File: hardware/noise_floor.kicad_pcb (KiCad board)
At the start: 2 copper layers, 51.5 x 62.1 mm, 14 parts, among them J1 Input, J2 Output, J3 DC Power, J4 IO/Effect Connector 1 (IO Sid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, J5 IO/Effect Connector 2 (IO Sid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, J6 IO/Switch Connector 1 (IO Sid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, J7 IO/Switch Connector 2 (IO Sid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, J8 IO/Switch Connector 1 (Switch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, J9 IO/Switch Connector 2 (Switch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, SW1 Footswitch

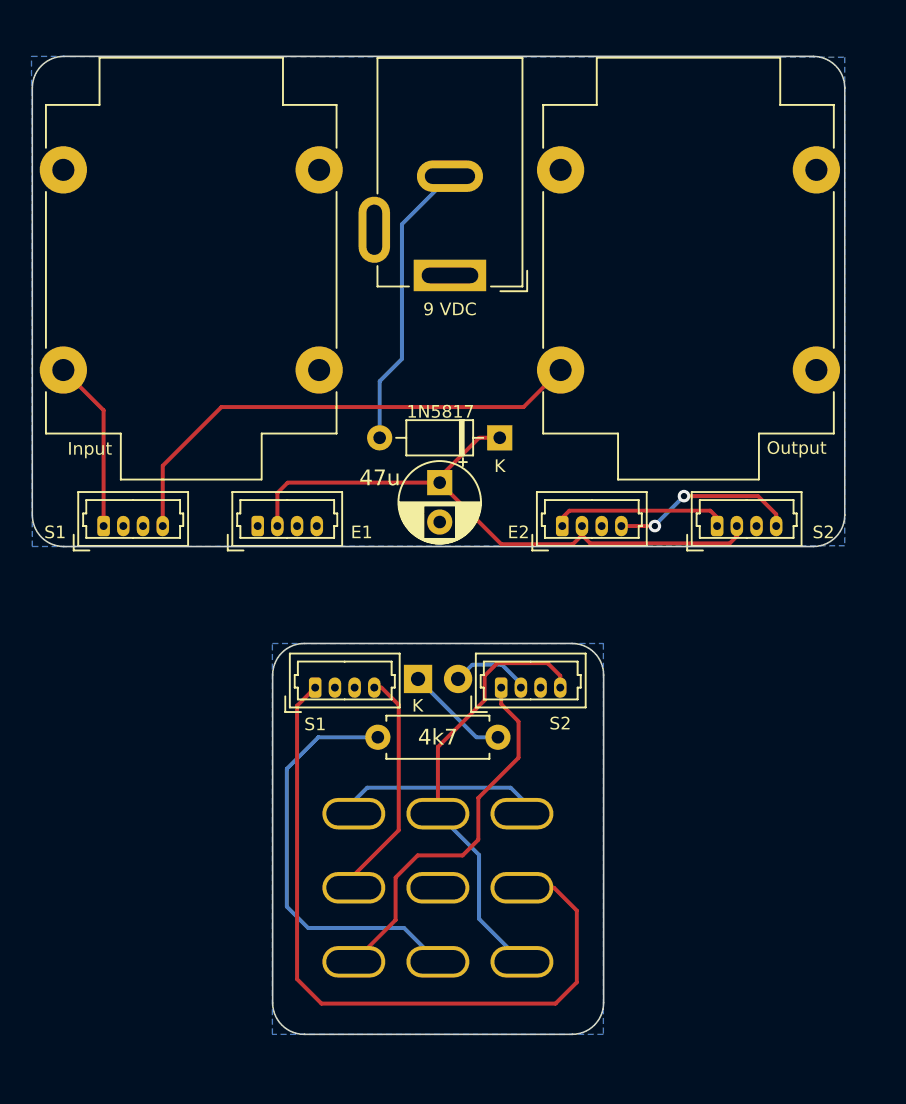
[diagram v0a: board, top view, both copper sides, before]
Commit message: v0.03 updates:
 - switch to SMD resistor and diode to save space (particularly on footswitch board)
 - move IO and DC jacks to bottom of board and ensure they're on the correct side
 - consolidate to a single effect board connector.
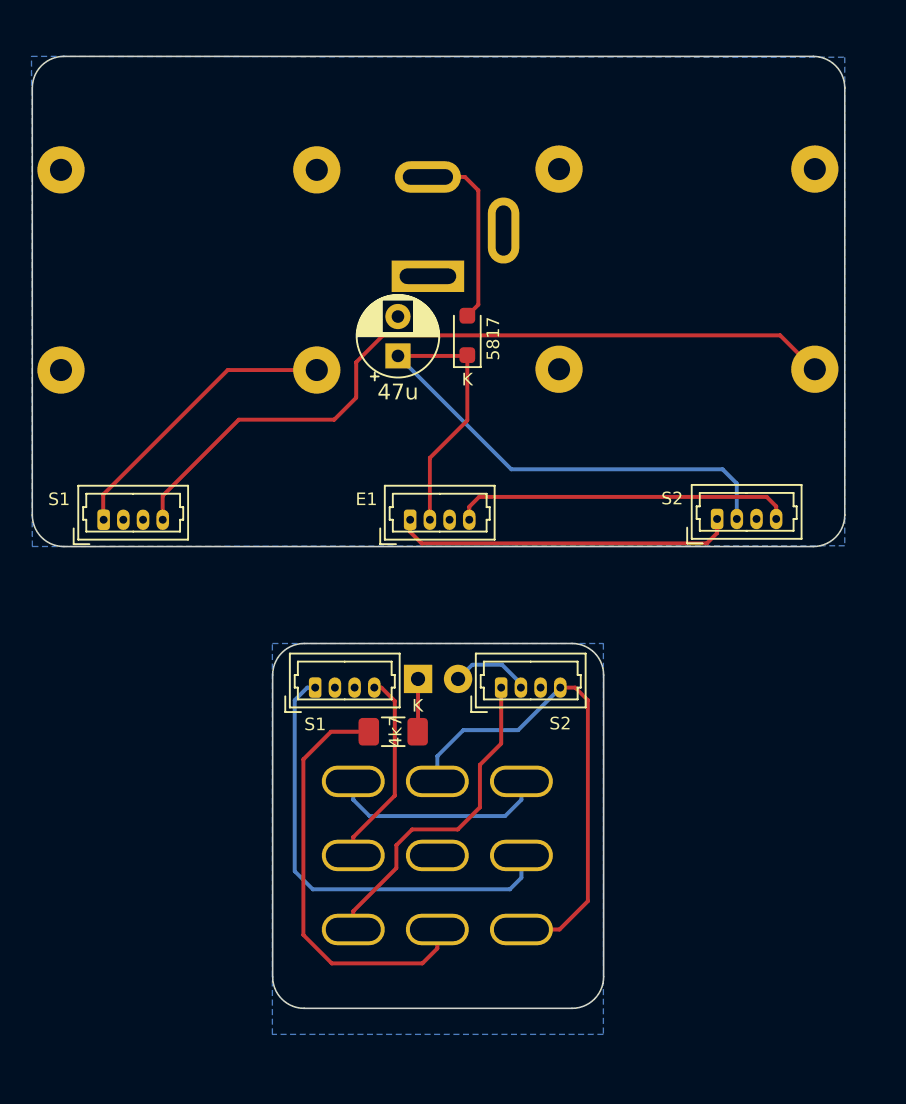
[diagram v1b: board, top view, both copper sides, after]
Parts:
- removed the J4 at (29.2, 45.1)
- D2: renamed from D1; value 1N5817 -> B5817WS; footprint Diode_THT:D_DO-35_SOD27_P7.62mm_Horizontal -> Diode_SMD:D_SOD-323_HandSoldering
- J1, J2, J3: moved to B.Cu
- J4: renamed from J5; value IO/Effect Connector 2 (IO Side) [E2] -> IO/Effect Connector 1 (IO Side) [E1]
- R1: footprint Resistor_THT:R_Axial_DIN0207_L6.3mm_D2.5mm_P7.62mm_Horizontal -> Resistor_SMD:R_1206_3216Metric_Pad1.30x1.75mm_HandSolder
- moved J2 16.1 mm to (64.6, 35.2)
- moved J1 16.1 mm to (33.0, 35.2)
- moved J4 9.66 mm to (38.9, 44.8)
- moved C1 8.47 mm to (38.1, 34.4), turned to 90 degrees
- moved D2 6.81 mm to (42.5, 33.1), turned to 90 degrees
- moved R1 6.65 mm to (37.9, 58.2)
- moved SW1 2.05 mm to (40.6, 66.0)
- moved J3 1.40 mm to (40.0, 29.3), turned to 0 degrees
- moved J6 0.45 mm to (58.4, 44.7)
- moved J5 0.40 mm to (19.5, 44.8)
- renumbered D2 to D1, J6 to J5, J7 to J6, J8 to J7, J9 to J8
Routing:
- net /OUTPUT_TIP_IO: track 31.6 -> 49.3 mm
- net /INPUT_TIP_SW: track 46.6 -> 29.1 mm
- net /EFFECT_OUTPUT_IO: track 11.3 -> 21.7 mm
- net /EFFECT_INPUT_IO: track 11.9 -> 21.3 mm, vias 2 -> 0
- net /INPUT_TIP_IO: track 11.0 -> 18.4 mm
- net /DC_SHIELD: track 18.4 -> 11.8 mm
- net Net-(D1-K): track 6.60 -> 3.32 mm
- net /EFFECT_INPUT_SW: track 27.8 -> 31.0 mm
- net /EFFECT_OUTPUT_SW: track 23.9 -> 20.9 mm
- net /9V0_IO: track 40.2 -> 42.9 mm
- net /OUTPUT_TIP_SW: track 14.8 -> 12.5 mm
- net Net-(SW1A-A1): track 13.1 -> 13.9 mm
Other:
- board size 51.5 x 62.1 mm -> 51.5 x 60.4 mm
- board text added: "${COMMENT1} ${REVISION}"
- board text removed: "${COMMENT1}"

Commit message: update gitignore, random inconsequential changes to accomodate splitting boards
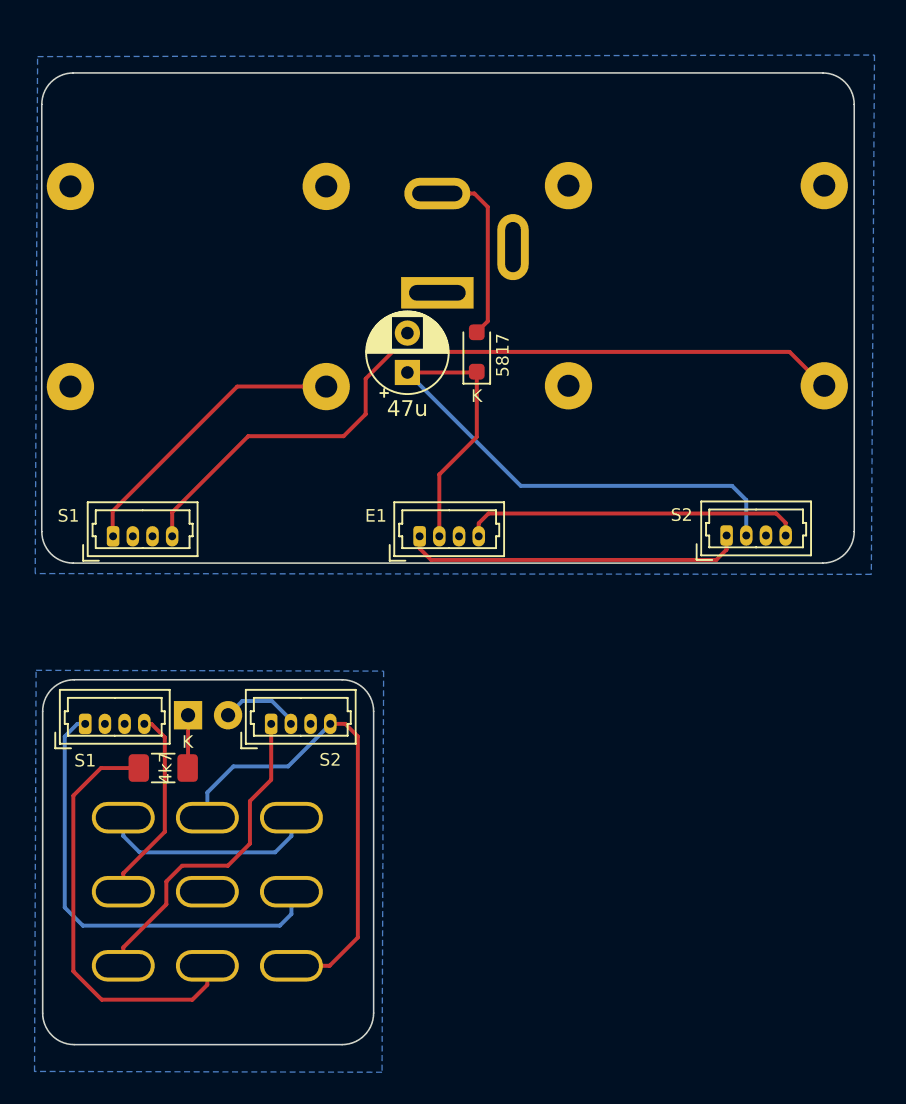
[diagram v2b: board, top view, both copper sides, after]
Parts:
- moved J8 14.8 mm to (30.1, 57.7)
- moved J7 14.8 mm to (18.3, 57.7)
- moved R1 14.8 mm to (23.3, 60.5)
- moved D1 14.8 mm to (24.8, 57.2)
- moved SW1 14.8 mm to (26.1, 68.4)
- moved D2 1.21 mm to (43.1, 34.1)
- moved J2 1.21 mm to (65.2, 36.2)
- moved J3 1.21 mm to (40.6, 30.4)
- moved C1 1.21 mm to (38.8, 35.4)
- moved J1 1.21 mm to (33.6, 36.3)
- moved J4 1.21 mm to (39.5, 45.8)
- moved J6 1.21 mm to (59.0, 45.8)
- moved J5 1.21 mm to (20.1, 45.8)
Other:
- board size 51.5 x 60.4 mm -> 51.5 x 61.7 mm

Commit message: Some updates based on feedback from freestompboxes.org folks:
 - Add back thermal reliefs on ground pads
 - Switch to stereo jacks for improved mechanical support
 - Use switched symbol/footprint for DC Barrel jack, correct circuit to suit (still need to add switching on input jack)
 - Add 3D models for various parts (courtesy of Vasily Kashirin - https://grabcad.com/vasily.kashirin-1/models?page=1)
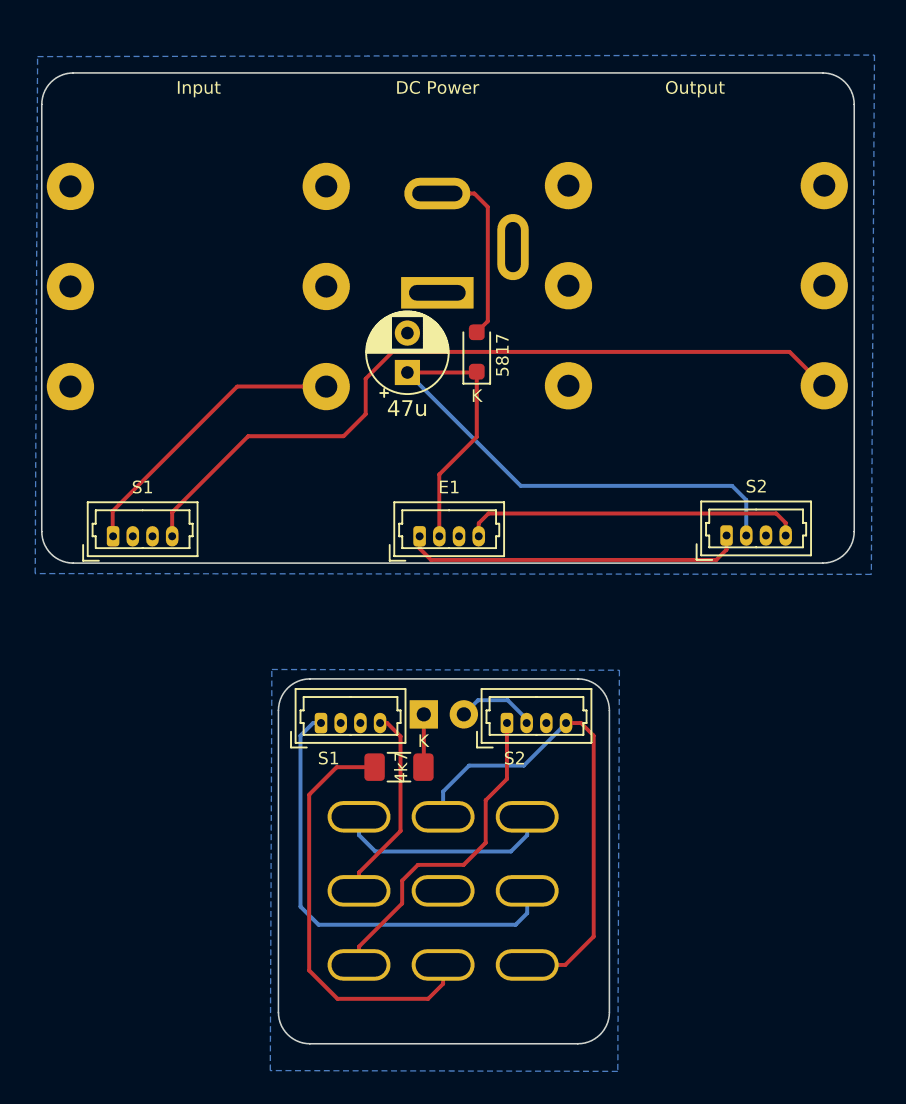
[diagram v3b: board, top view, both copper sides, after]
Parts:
- J1, J2: footprint Connector_Audio:Jack_6.35mm_Neutrik_NMJ4HCD2_Horizontal -> noise_floor:Jack_6.35mm_Neutrik_NMJ6HCD2_Horizontal-3DModel_from_Vasily_Kashirin
- J3: footprint Connector_BarrelJack:BarrelJack_GCT_DCJ200-10-A_Horizontal -> noise_floor:BarrelJack_GCT_DCJ200-10-A_Horizontal_with_3DModel_from_Vasily_Kashirin
- J4, J5, J6, J7, J8: footprint Connector_Molex:Molex_PicoBlade_53047-0410_1x04_P1.25mm_Vertical -> noise_floor:Molex_PicoBlade_53047-0410_1x04_P1.25mm_Vertical_with_3D_Model
- moved J8 15.0 mm to (45.1, 57.6)
- moved J7 15.0 mm to (33.3, 57.6)
- moved R1 15.0 mm to (38.2, 60.4)
- moved SW1 15.0 mm to (41.0, 68.3)
- moved D1 15.0 mm to (39.8, 57.1)
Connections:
- J3 pad 3: (no net) -> unconnected-(J3-Pad3)
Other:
- board size 51.5 x 61.7 mm -> 51.5 x 61.6 mm

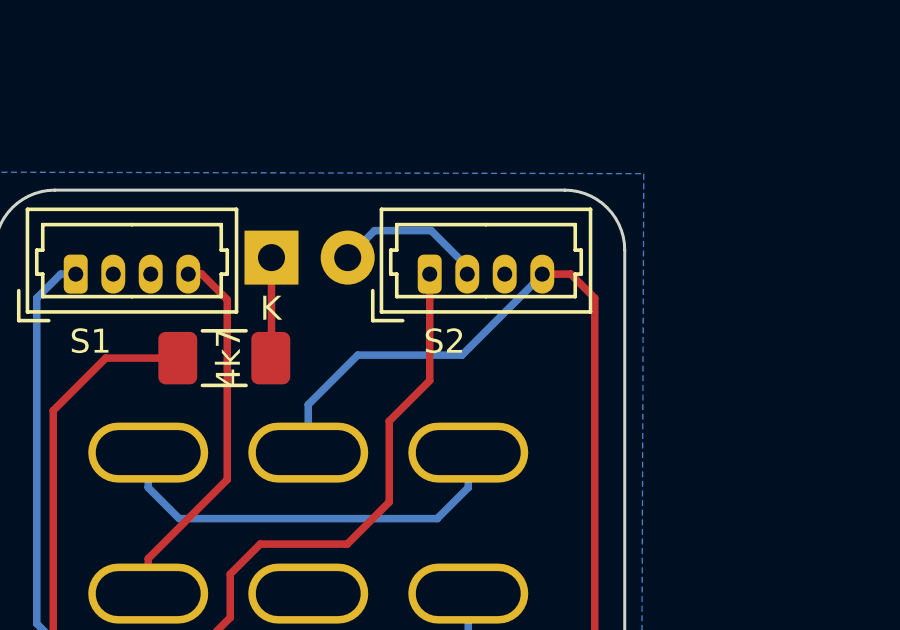
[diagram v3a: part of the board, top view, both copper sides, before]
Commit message: fix a couple DRCs and bump rev
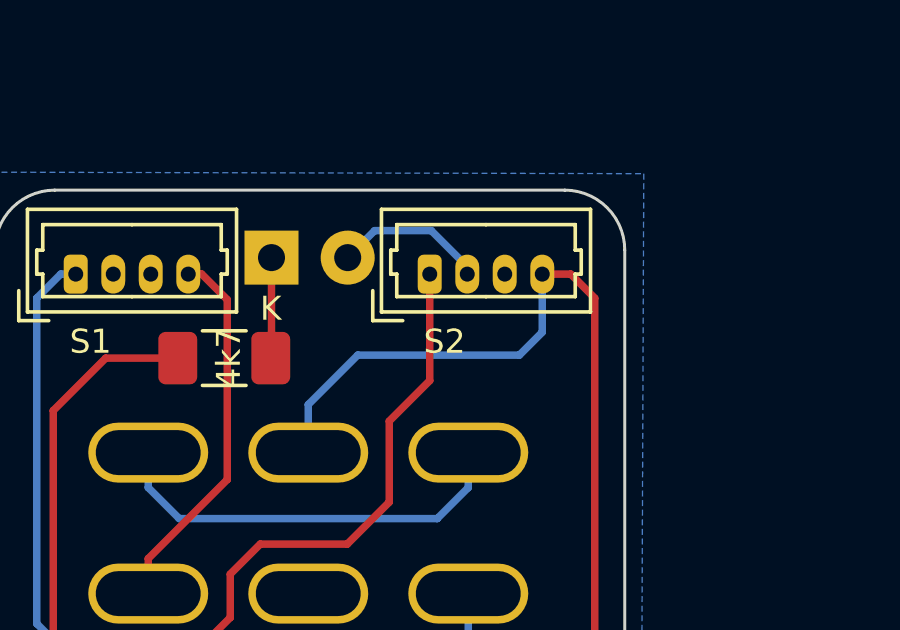
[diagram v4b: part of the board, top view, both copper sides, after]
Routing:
- net /EFFECT_INPUT_SW: track 31.0 -> 32.1 mm
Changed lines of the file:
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@@
   (title_block
     (title "Noise Floor Interface Boards")
-    (date "2023-03-03")
-    (rev "v0.03")
+    (date "2023-03-04")
+    (rev "v0.04")
     (comment 1 "github.com/whbeers/noise_floor")
   )
@@
       (rotate (xyz 0 0 0))
     )
-    (model "/home/whbeers/src-mine/stepfiles/530470410.stp"
+    (model "${KIPRJMOD}/noise_floor.pretty/530470410.stp"
       (offset (xyz 1.9 -1.15 5.5))
       (scale (xyz 1 1 1))
@@
       (rotate (xyz 0 0 0))
     )
-    (model "/home/whbeers/src-mine/stepfiles/530470410.stp"
+    (model "${KIPRJMOD}/noise_floor.pretty/530470410.stp"
       (offset (xyz 1.9 -1.15 5.5))
       (scale (xyz 1 1 1))
@@
       (rotate (xyz 0 0 0))
     )
-    (model "/home/whbeers/src-mine/stepfiles/530470410.stp"
+    (model "${KIPRJMOD}/noise_floor.pretty/530470410.stp"
       (offset (xyz 1.9 -1.15 5.5))
       (scale (xyz 1 1 1))
@@
       (rotate (xyz 0 0 0))
     )
-    (model "/home/whbeers/src-mine/stepfiles/530470410.stp"
+    (model "${KIPRJMOD}/noise_floor.pretty/530470410.stp"
       (offset (xyz 1.9 -1.15 5.5))
       (scale (xyz 1 1 1))
@@
       (rotate (xyz 0 0 0))
     )
-    (model "/home/whbeers/src-mine/stepfiles/530470410.stp"
+    (model "${KIPRJMOD}/noise_floor.pretty/530470410.stp"
       (offset (xyz 1.9 -1.15 5.5))
       (scale (xyz 1 1 1))
@@
         (effects (font (size 1 1) (thickness 0.15)) (justify mirror))
     )
-    (fp_text value "Input" (at 18.95 -8.1) (layer "F.SilkS" knockout)
+    (fp_text value "Input" (at 18.95 -8.1) (layer "F.SilkS")
         (effects (font (size 0.8 0.8) (thickness 0.15)))
     )
@@
       (rotate (xyz 0 0 0))
     )
-    (model "/home/whbeers/src-mine/stepfiles/NMJ6HCD2.step"
+    (model "${KIPRJMOD}/noise_floor.pretty/NMJ6HCD2.step"
       (offset (xyz 6.3 -8.1 0.5))
       (scale (xyz 1 1 1))
@@
     (pad "9" thru_hole oval (at 5.334 -4.699 180) (size 4 2) (drill oval 3.5 1.5) (layers "*.Cu" "*.Mask")
       (net 13 "/EFFECT_OUTPUT_SW") (pinfunction "C3") (pintype "passive"))
-    (model "/home/whbeers/src-mine/stepfiles/SF17020F-0302-21R-L.step"
+    (model "${KIPRJMOD}/noise_floor.pretty/SF17020F-0302-21R-L.step"
       (offset (xyz 0 0 0))
       (scale (xyz 1 1 1))
@@
         (effects (font (size 1 1) (thickness 0.15)) (justify mirror))
     )
-    (fp_text value "DC Power" (at 0 -13 180) (layer "F.SilkS" knockout)
+    (fp_text value "DC Power" (at 0 -13 180) (layer "F.SilkS")
         (effects (font (size 0.8 0.8) (thickness 0.15)))
     )
@@
       (rotate (xyz 0 0 0))
     )
-    (model "/home/whbeers/src-mine/stepfiles/DS-210.step"
+    (model "${KIPRJMOD}/noise_floor.pretty/DS-210.step"
       (offset (xyz 0 -14.9 0.5))
       (scale (xyz 1 1.1 1))
@@
         (effects (font (size 1 1) (thickness 0.15)) (justify mirror))
     )
-    (fp_text value "Output" (at 18.9 -8.2) (layer "F.SilkS" knockout)
+    (fp_text value "Output" (at 18.9 -8.2) (layer "F.SilkS")
         (effects (font (size 0.8 0.8) (thickness 0.15)))
     )
@@
       (rotate (xyz 0 0 0))
     )
-    (model "/home/whbeers/src-mine/stepfiles/NMJ6HCD2.step"
+    (model "${KIPRJMOD}/noise_floor.pretty/NMJ6HCD2.step"
       (offset (xyz 6.3 -8.1 0.5))
       (scale (xyz 1 1 1))
@@
   (segment (start 46.35 72.996) (end 48.768 72.996) (width 0.25) (layer "F.Cu") (net 10))
   (segment (start 50.566 71.198) (end 50.566 58.448) (width 0.25) (layer "F.Cu") (net 10))
+  (segment (start 41.016 61.998) (end 41.016 63.598) (width 0.25) (layer "B.Cu") (net 10))
+  (segment (start 48.816 57.673305) (end 48.816 59.584) (width 0.25) (layer "B.Cu") (net 10))
+  (segment (start 48.052 60.348) (end 42.666 60.348) (width 0.25) (layer "B.Cu") (net 10))
+  (segment (start 48.816 59.584) (end 48.052 60.348) (width 0.25) (layer "B.Cu") (net 10))
   (segment (start 42.666 60.348) (end 41.016 61.998) (width 0.25) (layer "B.Cu") (net 10))
-  (segment (start 48.816 57.673305) (end 46.141305 60.348) (width 0.25) (layer "B.Cu") (net 10))
-  (segment (start 46.141305 60.348) (end 42.666 60.348) (width 0.25) (layer "B.Cu") (net 10))
-  (segment (start 41.016 61.998) (end 41.016 63.598) (width 0.25) (layer "B.Cu") (net 10))
   (segment (start 39.416 66.648) (end 38.416 67.648) (width 0.25) (layer "F.Cu") (net 13))
   (segment (start 43.716 62.548) (end 43.716 65.248) (width 0.25) (layer "F.Cu") (net 13))
